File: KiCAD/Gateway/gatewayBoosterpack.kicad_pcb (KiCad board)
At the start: 2 copper layers, 47 x 49.5 mm, 13 parts

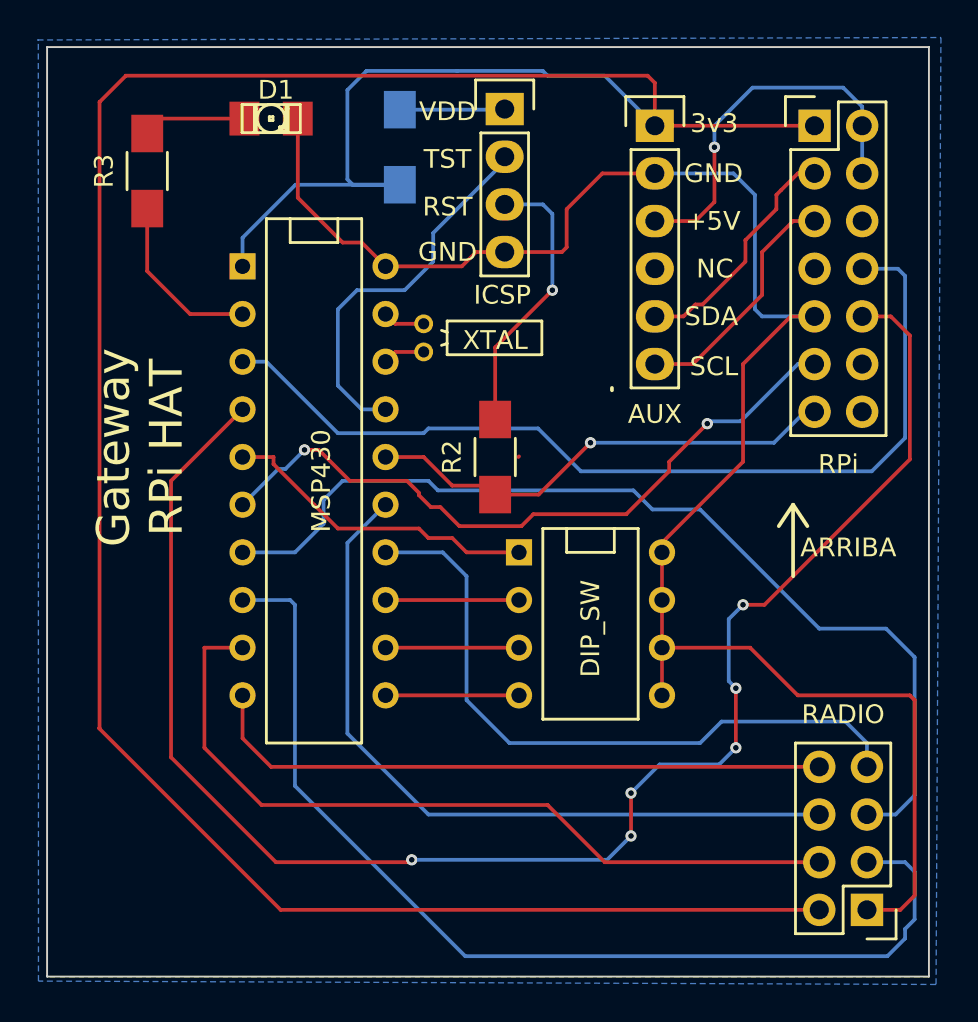
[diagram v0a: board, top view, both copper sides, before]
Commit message: Gateway PCB sent to SeeedStudio
PCB sent to manufacturing service.
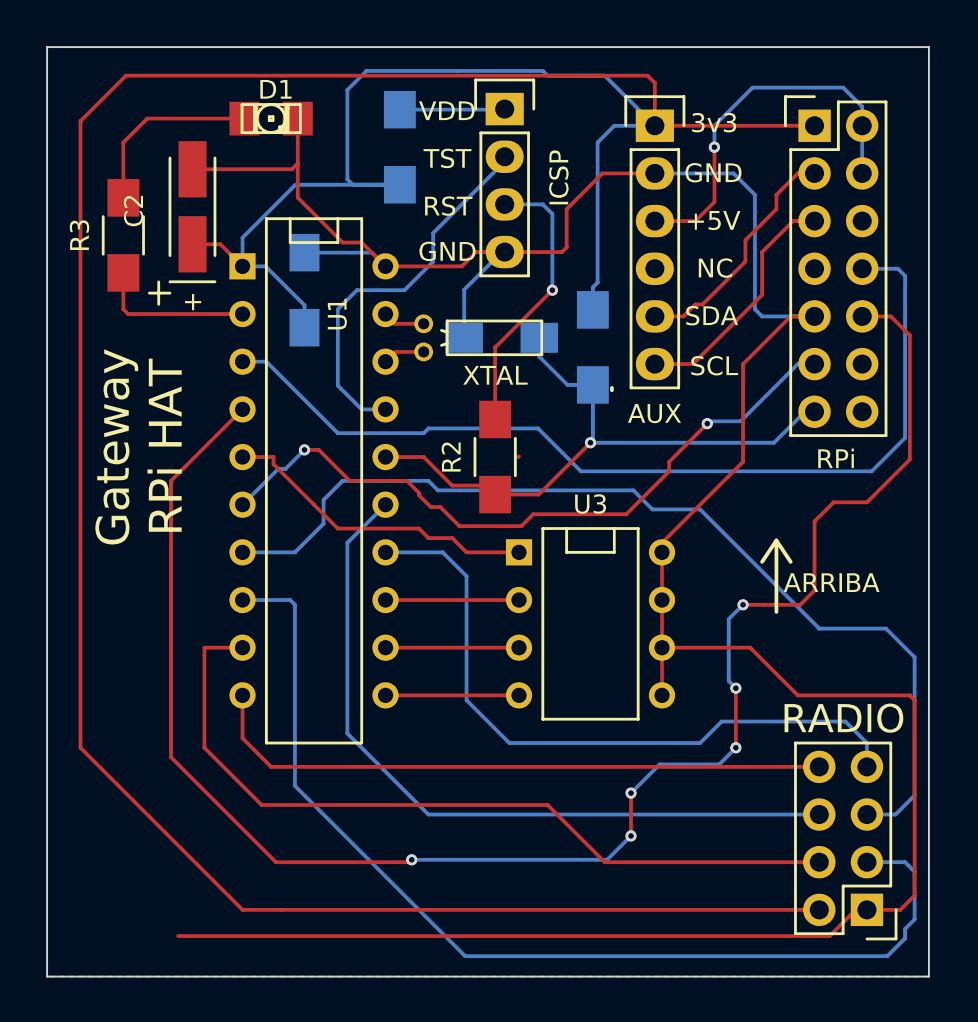
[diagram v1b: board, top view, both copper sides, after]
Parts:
- removed DIP_SW: DIP_SW, Housings_DIP:DIP-8__300
- removed MSP430: MSP430G2553, Housings_DIP:DIP-20__300
- added C1: 10nF, Capacitors_SMD:C_1206_HandSoldering, B.Cu at (127.1, 65.0)
- added C2: 10uF, Capacitors_Tantalum_SMD:TantalC_SizeA_EIA-3216_HandSoldering, F.Cu at (110.6, 58.0)
- added C3: 100nF, Capacitors_SMD:C_1206_HandSoldering, B.Cu at (116.6, 62.5)
- added R4: 47k, Resistors_SMD:R_1206_HandSoldering, B.Cu at (132.0, 65.5)
- added U1: MSP430G2553, Housings_DIP:DIP-20__300, F.Cu at (117.1, 72.6)
- added U3: DIP_SW_4, Housings_DIP:DIP-8__300, F.Cu at (131.8, 80.3)
- ICSP: value (none) -> PGM_MSP430
- R2: value 270 -> 220
- R3: value 1k -> 220
- moved R3 3.66 mm to (106.9, 59.6)
- moved G*** 1.15 mm to (134.2, 92.1)
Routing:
- net GND: track 95.4 -> 148.8 mm
- net +3V3: track 153.7 -> 176.6 mm
- net /RST_IN_MSP430: track 25.5 -> 33.1 mm
- net Net-(D1-Pad1): track 5.51 -> 9.93 mm
- net /RX_RPi: track 86.2 -> 88.3 mm
- net Net-(R3-Pad1): track 9.36 -> 8.39 mm
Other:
- board text added: "Ing. Iván René Morales Marconi Lab, ICTP Abril 2015"
- board text added: "Lab. C.C. Aplicadas Arquitectura USAC"
- board text added: "USAC"
- board text removed: "Ing. Ivan René Morales Marconi Lab, ICTP Abril 2015"
- board text removed: "Lab. CC. Aplicadas Arquitectura USAC"
